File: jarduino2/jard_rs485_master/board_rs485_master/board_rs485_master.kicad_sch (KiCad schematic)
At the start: 0 parts

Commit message: Finalisation dossier
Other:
- note added: "Alimentation"
- note added: "BUS RS485 + Sortie alim 12V"
- note added: "CPU"
- note added: "Commande des OYAs - Maître RS485"
- note added: "Maître des OYAS"
- note added: "Wifi"
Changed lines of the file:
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@@
   (title_block
     (title "Commande des OYA - Maître RS485")
-    (date "2024-03-30")
+    (date "2024-03-31")
     (rev "A0")
     (company "BPC")
@@
     (comment 4 "Maître RS485 avec alim 12 V commutée")
   )
-  (sheet (at 62.23 69.85) (size 43.18 86.36) (fields_autoplaced)
+  (text "BUS RS485 + Sortie alim 12V" (at 130.81 139.7 0)
+    (effects (font (face "Arial") (size 4 4) bold) (justify left bottom))
+  )
+  (text "Wifi" (at 205.74 97.79 0)
+    (effects (font (face "Arial") (size 4 4) bold) (justify left bottom))
+  )
+  (text "Alimentation" (at 72.39 110.49 0)
+    (effects (font (face "Arial") (size 4 4) bold) (justify left bottom))
+  )
+  (text "Commande des OYAs - Maître RS485" (at 88.9 45.72 0)
+    (effects (font (face "Arial") (size 5 5) bold) (justify left bottom))
+  )
+  (text "Maître des OYAS" (at 93.98 36.83 0)
+    (effects (font (face "Arial") (size 10 10) (thickness 0.4) bold) (justify left bottom))
+  )
+  (text "CPU" (at 148.59 96.52 0)
+    (effects (font (face "Arial") (size 4 4) bold) (justify left bottom))
+  )
+  (sheet (at 68.58 67.31) (size 43.18 83.82) (fields_autoplaced)
     (stroke (width 0.1524) (type solid))
     (fill (color 0 0 0 0.0000))
-    (property "Sheetname" "Power" (at 62.23 69.1384 0)
+    (property "Sheetname" "Power" (at 68.58 66.5984 0)
       (effects (font (size 1.27 1.27)) (justify left bottom))
     )
-    (property "Sheetfile" "power.kicad_sch" (at 62.23 156.7946 0)
+    (property "Sheetfile" "power.kicad_sch" (at 68.58 151.7146 0)
       (effects (font (size 1.27 1.27)) (justify left top))
     )
@@
     )
   )
-  (sheet (at 218.44 100.33) (size 29.21 19.05) (fields_autoplaced)
+  (sheet (at 199.39 68.58) (size 22.86 52.07) (fields_autoplaced)
     (stroke (width 0.1524) (type solid))
     (fill (color 0 0 0 0.0000))
-    (property "Sheetname" "Wifi" (at 218.44 99.6184 0)
+    (property "Sheetname" "Wifi" (at 199.39 67.8684 0)
       (effects (font (size 1.27 1.27)) (justify left bottom))
     )
-    (property "Sheetfile" "wifi.kicad_sch" (at 218.44 119.9646 0)
+    (property "Sheetfile" "wifi.kicad_sch" (at 199.39 121.2346 0)
       (effects (font (size 1.27 1.27)) (justify left top))
     )
-    (property "Field2" "" (at 218.44 100.33 0)
+    (property "Field2" "" (at 199.39 68.58 0)
       (effects (font (size 1.27 1.27)) hide)
     )
@@
     )
   )
-  (sheet (at 109.22 125.73) (size 107.95 27.94) (fields_autoplaced)
+  (sheet (at 115.57 123.19) (size 107.95 27.94) (fields_autoplaced)
     (stroke (width 0.1524) (type solid))
     (fill (color 0 0 0 0.0000))
-    (property "Sheetname" "Bus" (at 109.22 125.0184 0)
+    (property "Sheetname" "Bus" (at 115.57 122.4784 0)
       (effects (font (size 1.27 1.27)) (justify left bottom))
     )
-    (property "Sheetfile" "bus.kicad_sch" (at 109.22 154.2546 0)
+    (property "Sheetfile" "bus.kicad_sch" (at 115.57 151.7146 0)
       (effects (font (size 1.27 1.27)) (justify left top))
     )
-    (property "Champ2" "" (at 109.22 125.73 0)
+    (property "Champ2" "" (at 115.57 123.19 0)
       (effects (font (size 1.27 1.27)) hide)
     )
@@
     )
   )
-  (sheet (at 109.22 71.12) (size 106.68 52.07) (fields_autoplaced)
+  (sheet (at 115.57 68.58) (size 81.28 52.07)
     (stroke (width 0.1524) (type solid))
     (fill (color 0 0 0 0.0000))
-    (property "Sheetname" "cpu" (at 109.22 70.4084 0)
+    (property "Sheetname" "cpu" (at 115.57 67.8684 0)
       (effects (font (size 1.27 1.27)) (justify left bottom))
     )
-    (property "Sheetfile" "cpu.kicad_sch" (at 109.22 123.7746 0)
+    (property "Sheetfile" "cpu.kicad_sch" (at 176.53 120.65 0)
       (effects (font (size 1.27 1.27)) (justify left top))
     )

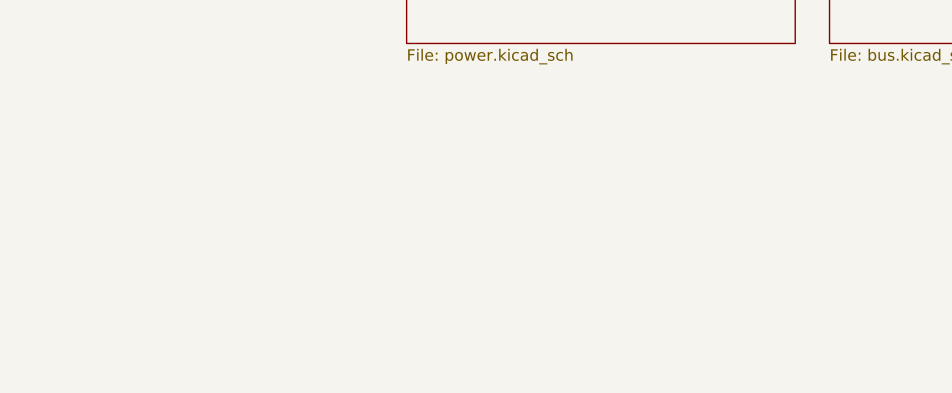
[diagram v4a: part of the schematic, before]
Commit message: Amélioration suite remise en route:
  - Agrandissement trous des LEDs D1 et D3
  - Correction erreur type du MOS P GDS
  - Agrandissement empreintes de R5,R7,R13 et R10 + verticales
  - Ajout de la description des opérations de rework pour le MOD485
  - Ajout d'une interface pour adapter le bus (5V, A, B et Gnd)
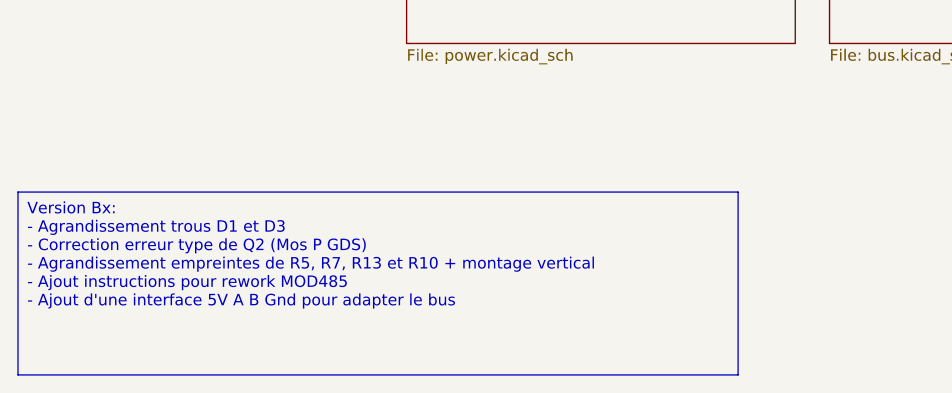
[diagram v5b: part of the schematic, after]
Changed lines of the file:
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@@
   (title_block
     (title "Commande des OYA - Maître RS485")
-    (date "2024-03-31")
-    (rev "A0")
+    (date "2024-04-09")
+    (rev "B0")
     (company "BPC")
     (comment 1 "Extension Wifi (ESP01)")
@@
     (comment 4 "Maître RS485 avec alim 12 V commutée")
   )
+  (text_box "Version Bx:\n  - Agrandissement trous D1 et D3\n  - Correction erreur type de Q2 (Mos P GDS)\n  - Agrandissement empreintes de R5, R7, R13 et R10 + montage vertical\n  - Ajout instructions pour rework MOD485\n  - Ajout d'une interface 5V A B Gnd pour adapter le bus\n"
+    (at 25.4 167.64 0) (size 80.01 20.32)
+    (stroke (width 0) (type default))
+    (fill (type none))
+    (effects (font (size 1.27 1.27)) (justify left top))
+  )
   (text "BUS RS485 + Sortie alim 12V" (at 130.81 139.7 0)

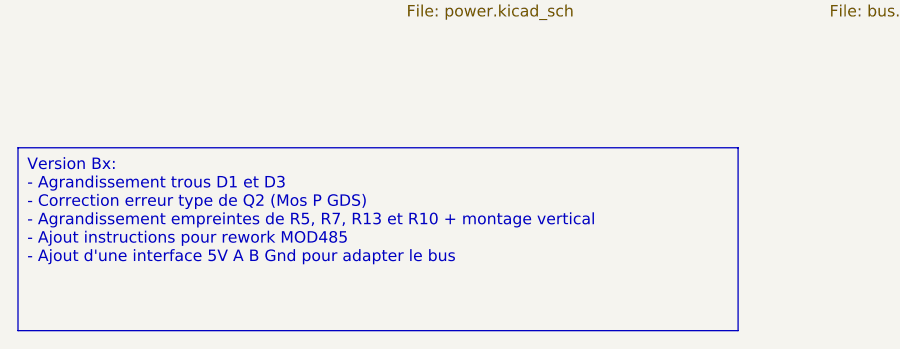
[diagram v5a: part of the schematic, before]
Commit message: Correction de l'inversion RX/TX du module Wifi
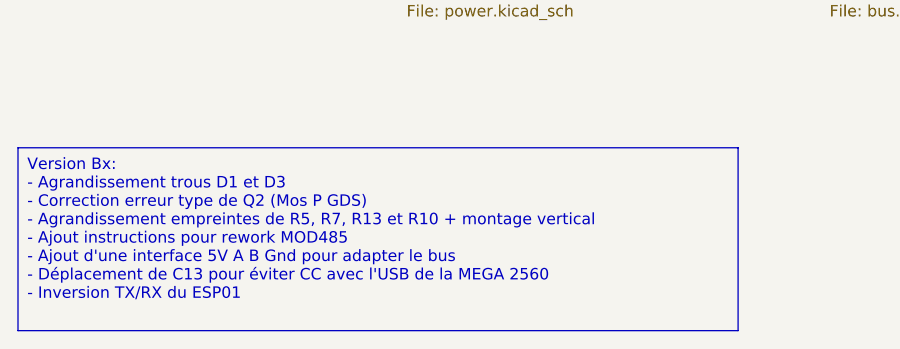
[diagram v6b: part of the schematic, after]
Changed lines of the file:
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@@
   (title_block
     (title "Commande des OYA - Maître RS485")
-    (date "2024-04-09")
+    (date "2024-04-24")
     (rev "B0")
     (company "BPC")
@@
     (comment 4 "Maître RS485 avec alim 12 V commutée")
   )
-  (text_box "Version Bx:\n  - Agrandissement trous D1 et D3\n  - Correction erreur type de Q2 (Mos P GDS)\n  - Agrandissement empreintes de R5, R7, R13 et R10 + montage vertical\n  - Ajout instructions pour rework MOD485\n  - Ajout d'une interface 5V A B Gnd pour adapter le bus\n"
+  (text_box "Version Bx:\n  - Agrandissement trous D1 et D3\n  - Correction erreur type de Q2 (Mos P GDS)\n  - Agrandissement empreintes de R5, R7, R13 et R10 + montage vertical\n  - Ajout instructions pour rework MOD485\n  - Ajout d'une interface 5V A B Gnd pour adapter le bus\n  - Déplacement de C13 pour éviter CC avec l'USB de la MEGA 2560\n  - Inversion TX/RX du ESP01\n"
     (at 25.4 167.64 0) (size 80.01 20.32)
     (stroke (width 0) (type default))

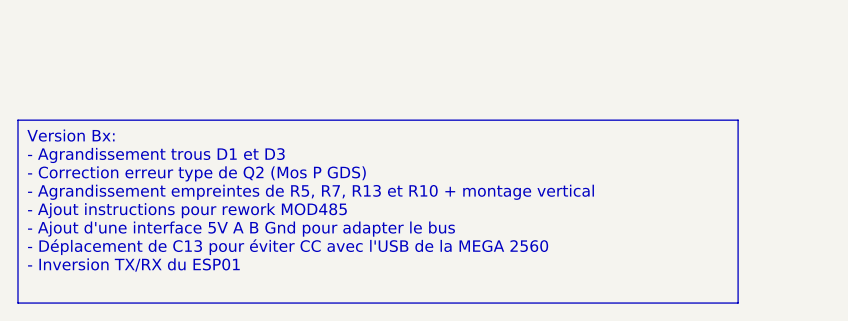
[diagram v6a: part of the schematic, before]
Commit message: Changement de la logique de commande des PWR Wifi et LEDs (avec un npn en plus)
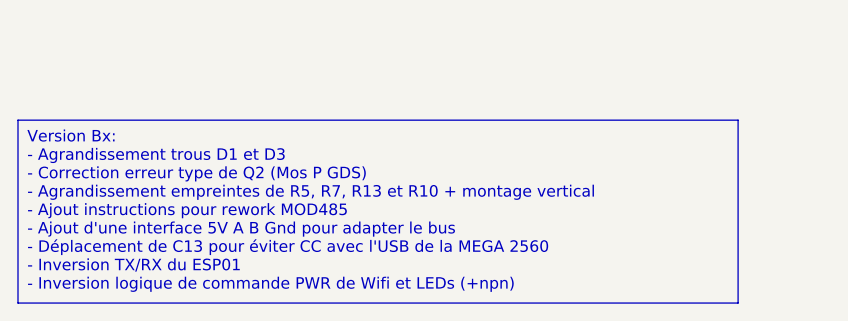
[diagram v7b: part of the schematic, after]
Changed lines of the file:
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@@
   (title_block
     (title "Commande des OYA - Maître RS485")
-    (date "2024-04-24")
+    (date "2024-04-26")
     (rev "B0")
     (company "BPC")
@@
     (comment 4 "Maître RS485 avec alim 12 V commutée")
   )
-  (text_box "Version Bx:\n  - Agrandissement trous D1 et D3\n  - Correction erreur type de Q2 (Mos P GDS)\n  - Agrandissement empreintes de R5, R7, R13 et R10 + montage vertical\n  - Ajout instructions pour rework MOD485\n  - Ajout d'une interface 5V A B Gnd pour adapter le bus\n  - Déplacement de C13 pour éviter CC avec l'USB de la MEGA 2560\n  - Inversion TX/RX du ESP01\n"
+  (text_box "Version Bx:\n  - Agrandissement trous D1 et D3\n  - Correction erreur type de Q2 (Mos P GDS)\n  - Agrandissement empreintes de R5, R7, R13 et R10 + montage vertical\n  - Ajout instructions pour rework MOD485\n  - Ajout d'une interface 5V A B Gnd pour adapter le bus\n  - Déplacement de C13 pour éviter CC avec l'USB de la MEGA 2560\n  - Inversion TX/RX du ESP01\n  - Inversion logique de commande PWR de Wifi et LEDs (+npn)\n"
     (at 25.4 167.64 0) (size 80.01 20.32)
     (stroke (width 0) (type default))

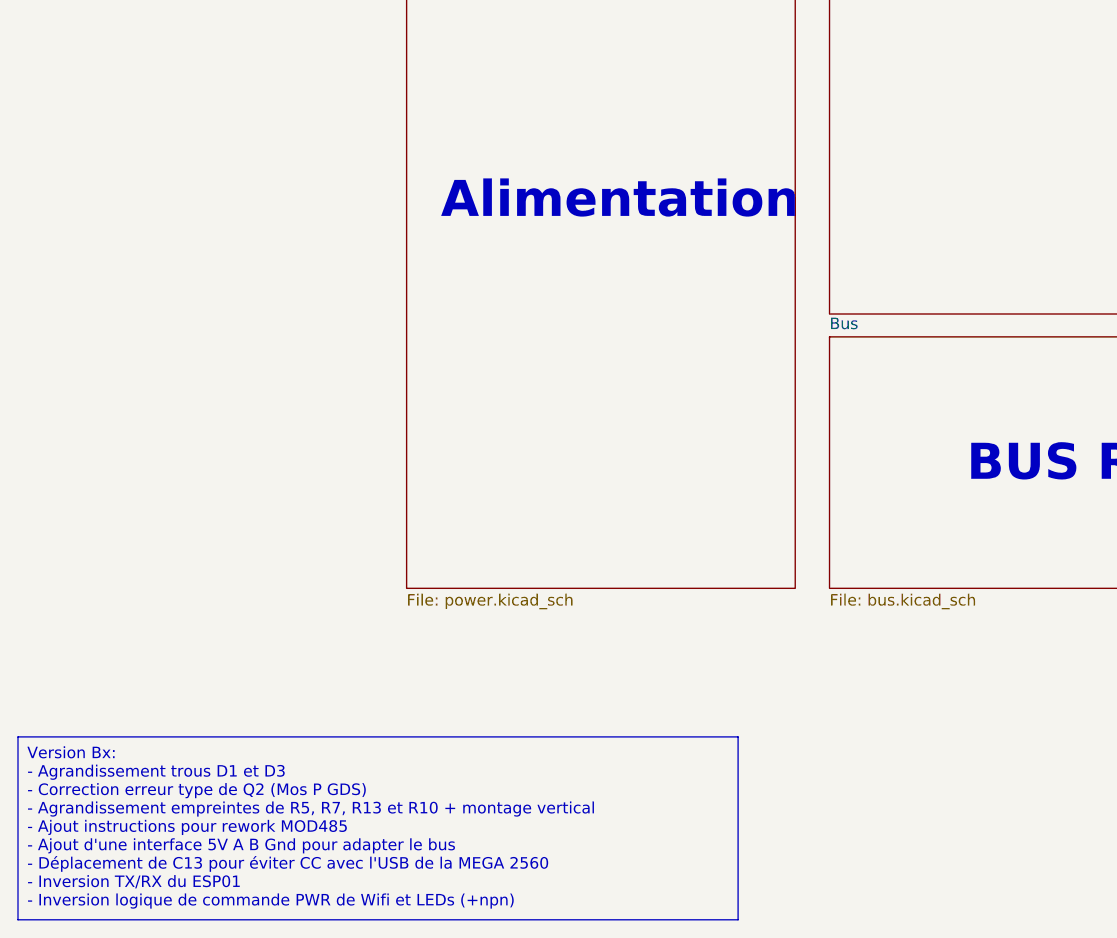
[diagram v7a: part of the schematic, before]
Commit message: Titres + finitions (vias)
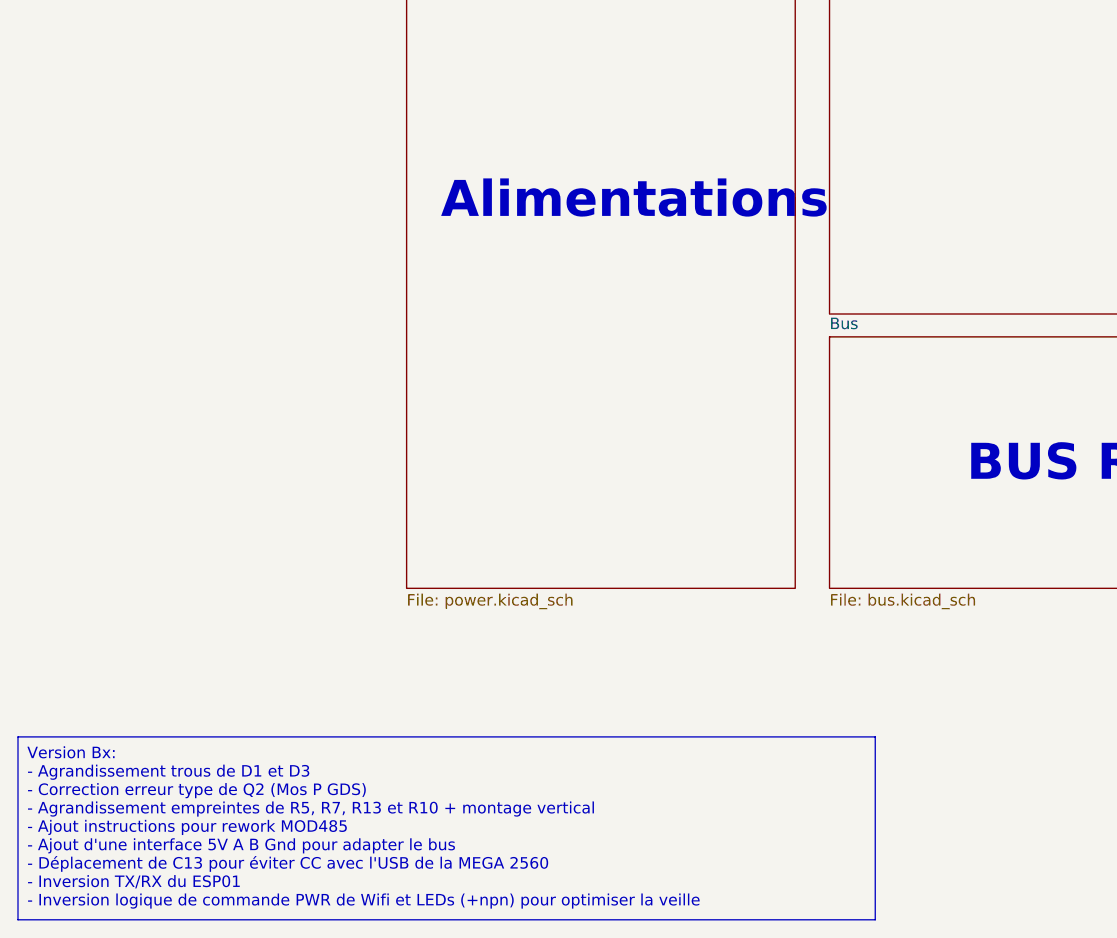
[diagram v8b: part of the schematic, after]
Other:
- note added: "Alimentations"
- note removed: "Alimentation"
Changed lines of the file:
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@@
     (comment 4 "Maître RS485 avec alim 12 V commutée")
   )
-  (text_box "Version Bx:\n  - Agrandissement trous D1 et D3\n  - Correction erreur type de Q2 (Mos P GDS)\n  - Agrandissement empreintes de R5, R7, R13 et R10 + montage vertical\n  - Ajout instructions pour rework MOD485\n  - Ajout d'une interface 5V A B Gnd pour adapter le bus\n  - Déplacement de C13 pour éviter CC avec l'USB de la MEGA 2560\n  - Inversion TX/RX du ESP01\n  - Inversion logique de commande PWR de Wifi et LEDs (+npn)\n"
-    (at 25.4 167.64 0) (size 80.01 20.32)
+  (text_box "Version Bx:\n  - Agrandissement trous de D1 et D3\n  - Correction erreur type de Q2 (Mos P GDS)\n  - Agrandissement empreintes de R5, R7, R13 et R10 + montage vertical\n  - Ajout instructions pour rework MOD485\n  - Ajout d'une interface 5V A B Gnd pour adapter le bus\n  - Déplacement de C13 pour éviter CC avec l'USB de la MEGA 2560\n  - Inversion TX/RX du ESP01\n  - Inversion logique de commande PWR de Wifi et LEDs (+npn) pour optimiser la veille\n"
+    (at 25.4 167.64 0) (size 95.25 20.32)
     (stroke (width 0) (type default))
     (fill (type none))
@@
     (effects (font (face "Arial") (size 4 4) bold) (justify left bottom))
   )
-  (text "Alimentation" (at 72.39 110.49 0)
+  (text "Alimentations" (at 72.39 110.49 0)
     (effects (font (face "Arial") (size 4 4) bold) (justify left bottom))
   )
